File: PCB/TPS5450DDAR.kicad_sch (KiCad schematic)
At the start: 11 parts, among them U8 TPS5450DDAR

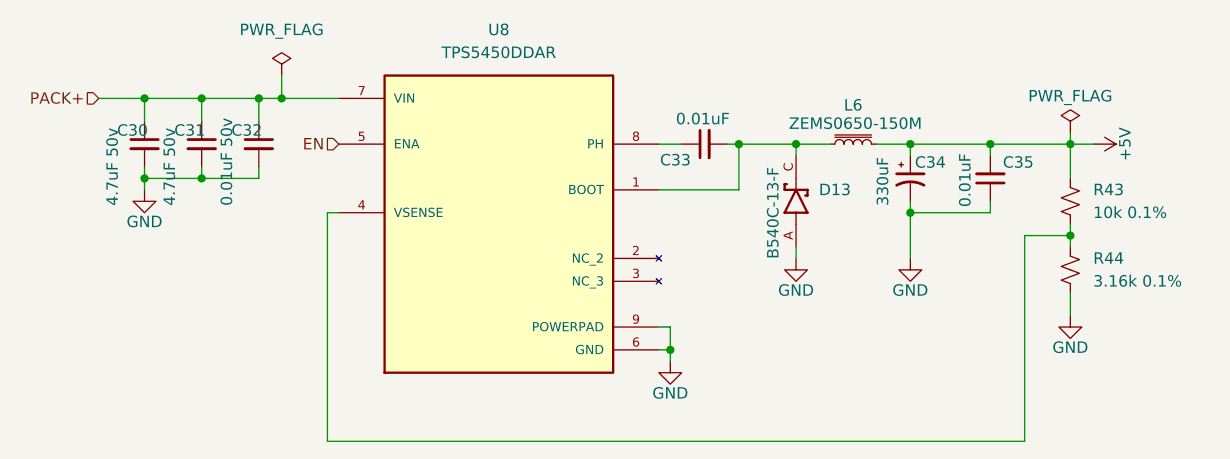
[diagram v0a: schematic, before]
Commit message: fix(PCB): 调优放电/预充电阻功率与母线采样布局
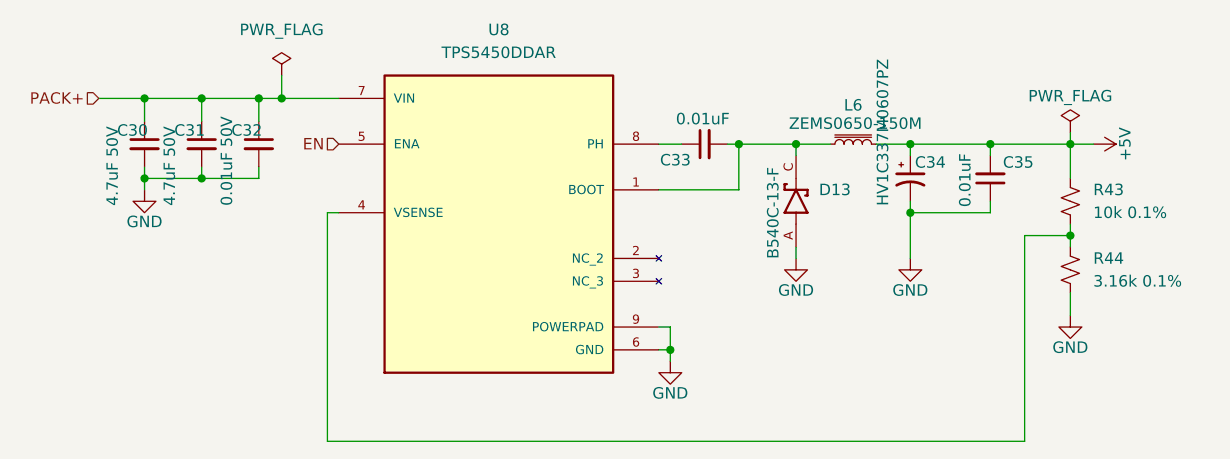
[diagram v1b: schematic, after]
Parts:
- C30, C31: value 4.7uF 50v -> 4.7uF 50V
- C32: value 0.01uF 50v -> 0.01uF 50V
- C34: value 330uF -> HV1C337M0607PZ
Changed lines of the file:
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@@
 			)
 		)
-		(property "Value" "4.7uF 50v"
+		(property "Value" "4.7uF 50V"
 			(at 115.824 94.488 90)
 			(effects
@@
 			)
 		)
-		(property "Value" "4.7uF 50v"
+		(property "Value" "4.7uF 50V"
 			(at 109.474 94.488 90)
 			(effects
@@
 			)
 		)
-		(property "Value" "330uF"
+		(property "Value" "HV1C337M0607PZ"
 			(at 195.072 94.488 90)
 			(effects
@@
 			)
 		)
-		(property "Value" "0.01uF 50v"
+		(property "Value" "0.01uF 50V"
 			(at 122.174 94.488 90)
 			(effects
